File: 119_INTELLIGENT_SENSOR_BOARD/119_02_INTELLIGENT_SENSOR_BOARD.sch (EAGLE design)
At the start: 14 parts

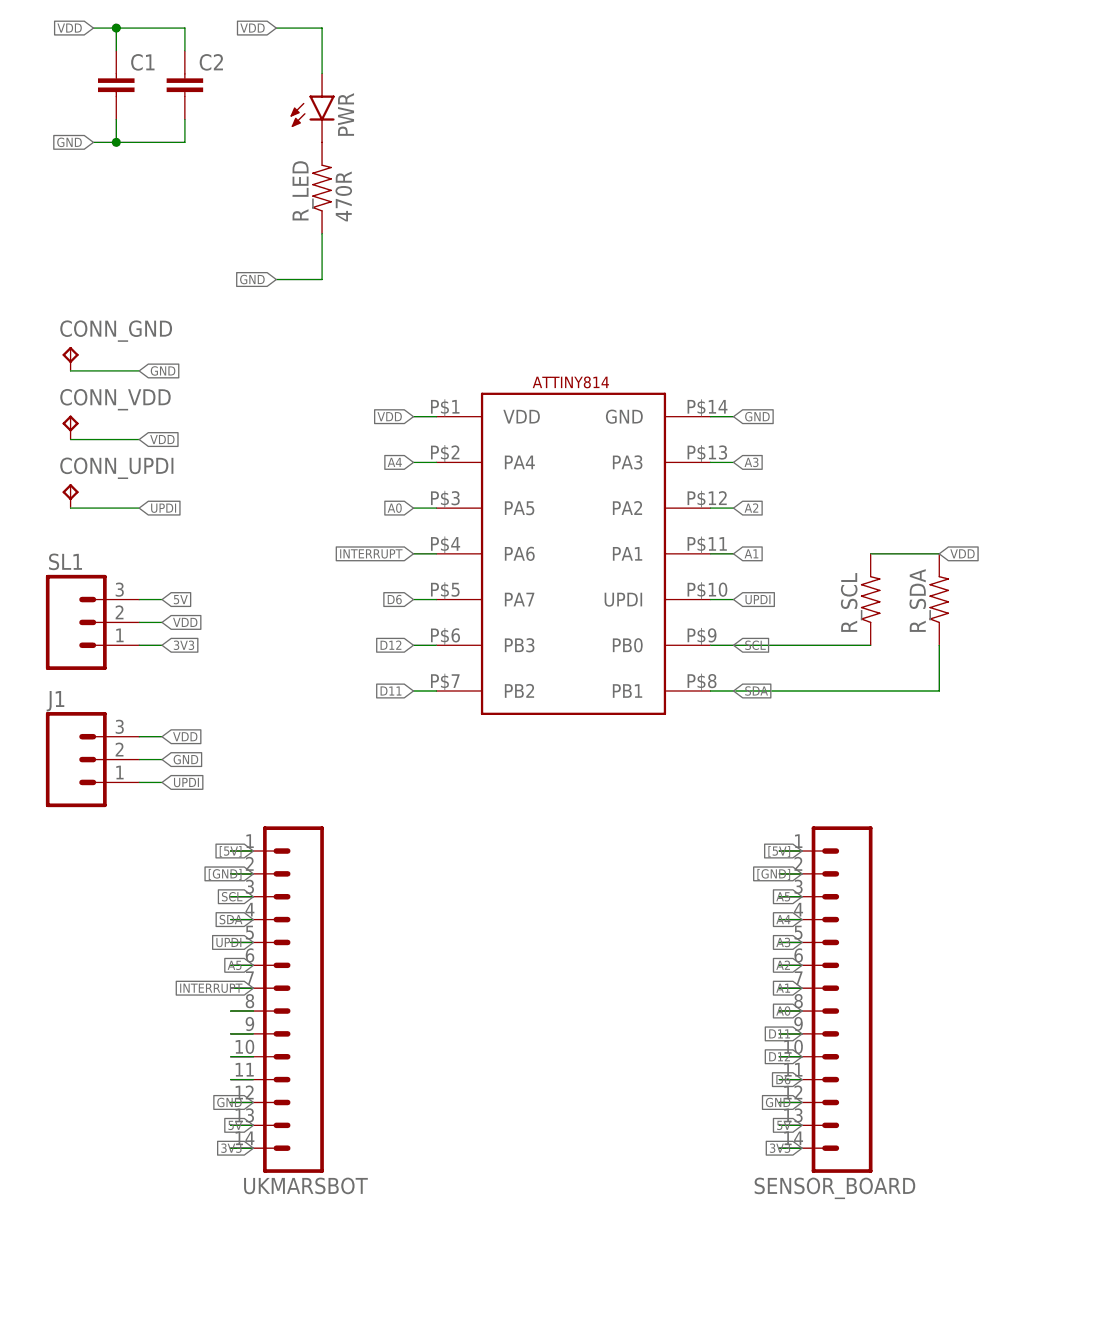
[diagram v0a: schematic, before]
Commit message: Formed new documentation
Split manual into datasheet, library and notes... added a few more ISC library header defines
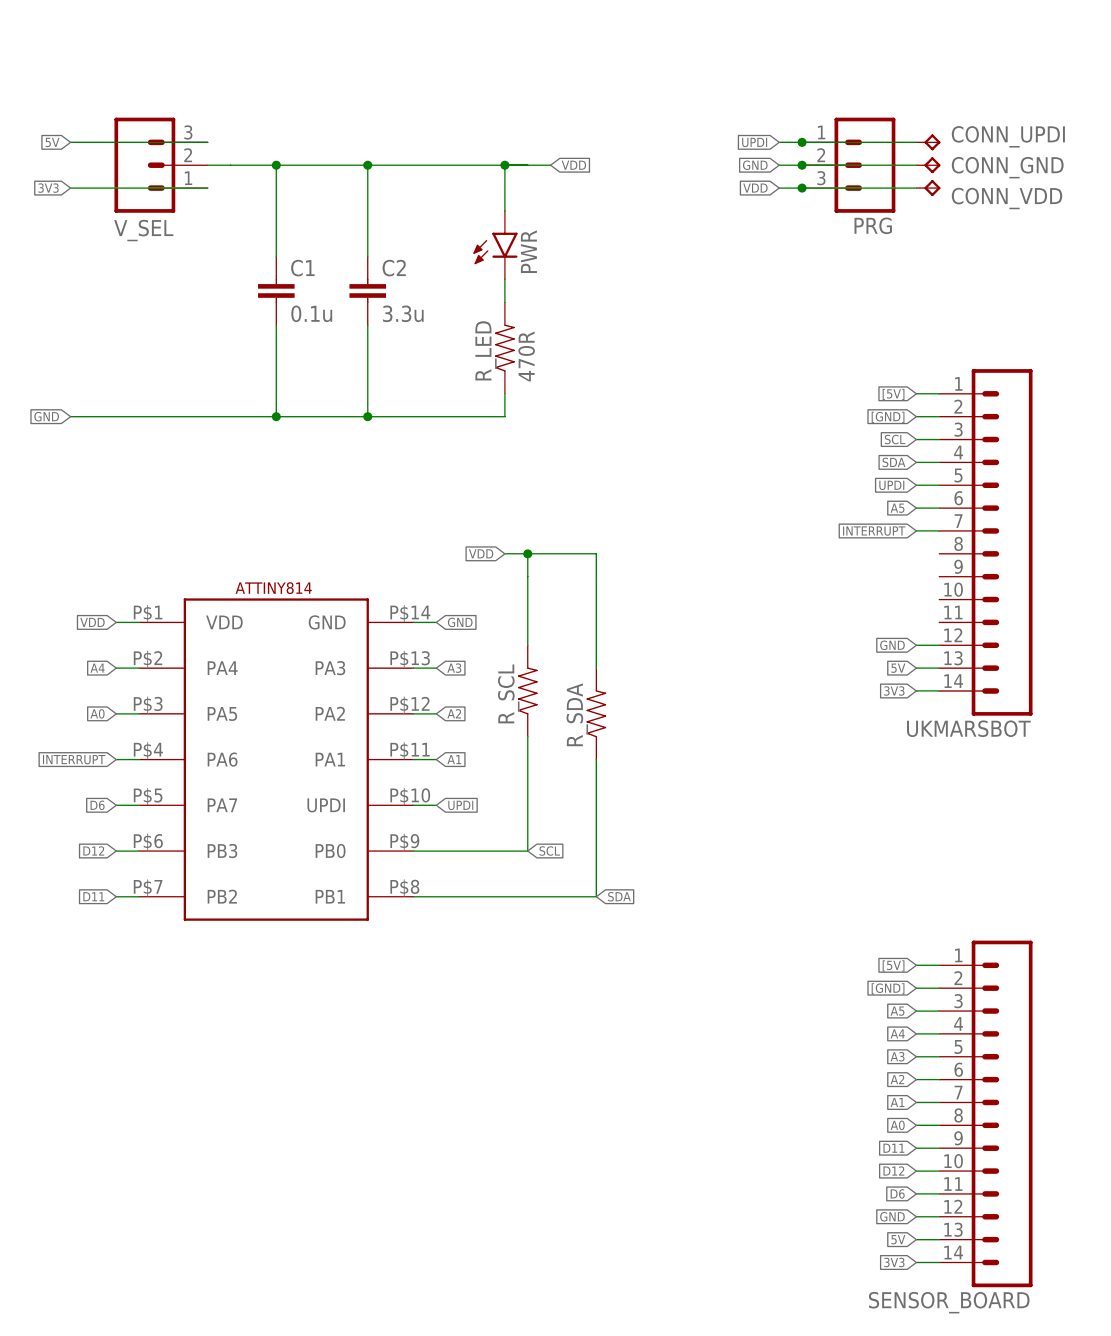
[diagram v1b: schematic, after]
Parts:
- removed J1, SL1: (no value), SparkFun-Connectors:M03PTH
- added PRG, V_SEL: (no value), SparkFun-Connectors:M03PTH
- C1: value (none) -> 0.1u
- C2: value (none) -> 3.3u
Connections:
- removed net N$10: UKMARSBOT.9
- removed net N$11: UKMARSBOT.11
- removed net N$15: UKMARSBOT.10
- removed net N$9: UKMARSBOT.8
- net 3V3: now also V_SEL.1; no longer SL1.1
- net 5V: now also V_SEL.3; no longer SL1.3
- net GND: now also PRG.2; no longer J1.2
- net UPDI: now also PRG.1; no longer J1.1
- net VDD: now also PRG.3, V_SEL.2; no longer J1.3, SL1.2
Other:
- note added: "Firmware Programming"
- note added: "ISC"
- note added: "Power Supply"
- note added: "Sensor Board Interface"
- note added: "UKMARSBOT Interface"
- moved on the sheet: C1, C2, CONN_GND, CONN_UPDI, CONN_VDD, PWR, R_LED, R_SCL, R_SDA, SENSOR_BOARD, UKMARSBOT
